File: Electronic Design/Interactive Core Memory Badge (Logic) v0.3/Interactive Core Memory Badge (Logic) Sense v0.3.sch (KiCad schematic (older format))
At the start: 22 parts, among them Q23 MMBT4401LT1G, Q24 MMBT4401LT1G, U3 LM393

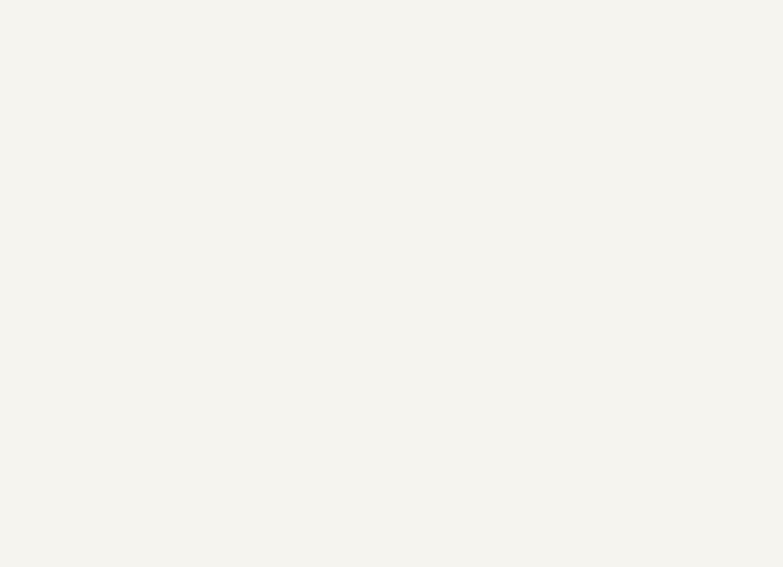
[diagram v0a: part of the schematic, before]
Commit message: Add I2C bus, clean-up power symbols, update MCU sheet.
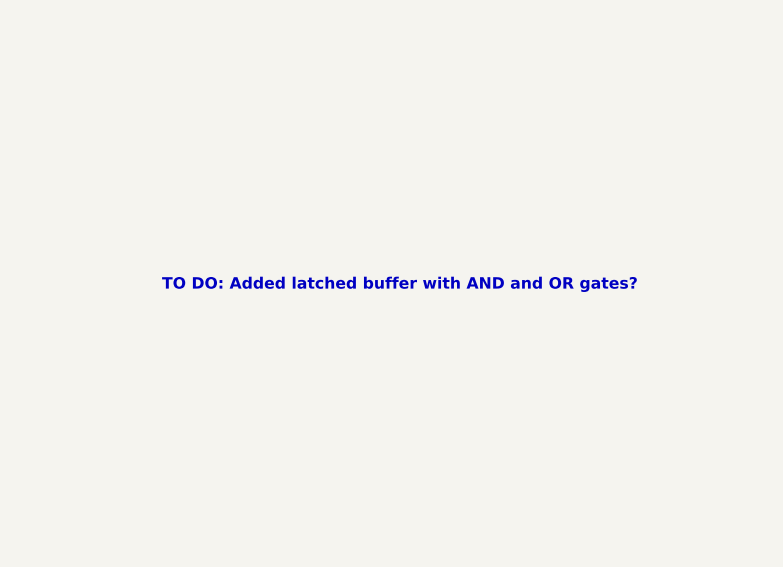
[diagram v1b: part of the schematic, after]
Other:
- note added: "TO DO: Added latched buffer with AND and OR gates?"
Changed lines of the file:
@@
 Connection ~ 3050 4850
 Connection ~ 3050 5450
+Text Notes 7200 3400 0    50   ~ 10
+TO DO: Added latched buffer with AND and OR gates?
 $EndSCHEMATC

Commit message: Add sense NORs and IO expansion and NOTs.
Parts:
- removed Q23, Q24: MMBT4401LT1G, Digikey:SOT-23-3, symbol Digikey-Transistors:MMBT4401LT1G
- removed R47: 10k, Resistor_SMD:R_0805_2012Metric, symbol Device:R
- added C7: 0.1uF, Capacitor_SMD:C_0805_2012Metric, symbol Device:CP1_Small
- added U4: 74HC02, symbol 74xx:74HC02
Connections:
- net labels added: 3V3_100mA, SENSE_RESET
- net labels removed: +3V3
- wire segments 63 -> 89
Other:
- note added: "SENSE SIGNAL RS LATCH"
- note removed: "SENSE SIGNAL BUFFER AND HOLD"
- note removed: "TO DO: Added latched buffer with AND and OR gates?"
- moved on the sheet: C4, C5, R36, R37, R38, R39, R40, R41, R42, R43, R44, R45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

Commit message: Schematic refinement
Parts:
- U4: footprint (none) -> Package_SO:SOIC-14_3.9x8.7mm_P1.27mm
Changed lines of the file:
@@
 $Descr A4 11693 8268
 encoding utf-8
-Sheet 5 6
+Sheet 3 5
 Title "Core 64 - Sense"
 Date "2020-03-15"
@@
 Comment4 ""
 $EndDescr
-Text Notes 550  700  0    118  ~ 0
+Text Notes 600  850  0    118  ~ 0
 SENSE SIGNAL PROCESSING
 $Comp
@@
 F 0 "U4" H 5100 2929 50  0000 C CNN
 F 1 "74HC02" H 5100 2836 50  0000 C CNN
-F 2 "" H 5100 2600 50  0001 C CNN
+F 2 "Package_SO:SOIC-14_3.9x8.7mm_P1.27mm" H 5100 2600 50  0001 C CNN
 F 3 "http://www.ti.com/lit/gpn/sn74hc02" H 5100 2600 50  0001 C CNN
 	1    5100 2600
@@
 F 0 "U4" H 5800 2929 50  0000 C CNN
 F 1 "74HC02" H 5800 2836 50  0000 C CNN
-F 2 "" H 5800 2600 50  0001 C CNN
+F 2 "Package_SO:SOIC-14_3.9x8.7mm_P1.27mm" H 5800 2600 50  0001 C CNN
 F 3 "http://www.ti.com/lit/gpn/sn74hc02" H 5800 2600 50  0001 C CNN
 	2    5800 2600
@@
 F 0 "U4" H 6500 2050 50  0000 C CNN
 F 1 "74HC02" H 6550 1950 50  0000 C CNN
-F 2 "" H 6600 1750 50  0001 C CNN
+F 2 "Package_SO:SOIC-14_3.9x8.7mm_P1.27mm" H 6600 1750 50  0001 C CNN
 F 3 "http://www.ti.com/lit/gpn/sn74hc02" H 6600 1750 50  0001 C CNN
 	3    6600 1750
@@
 F 0 "U4" H 6500 2800 50  0000 C CNN
 F 1 "74HC02" H 6550 2700 50  0000 C CNN
-F 2 "" H 6600 2500 50  0001 C CNN
+F 2 "Package_SO:SOIC-14_3.9x8.7mm_P1.27mm" H 6600 2500 50  0001 C CNN
 F 3 "http://www.ti.com/lit/gpn/sn74hc02" H 6600 2500 50  0001 C CNN
 	4    6600 2500
@@
 F 0 "U4" H 5380 3697 50  0000 L CNN
 F 1 "74HC02" H 5380 3604 50  0000 L CNN
-F 2 "" H 5150 3650 50  0001 C CNN
+F 2 "Package_SO:SOIC-14_3.9x8.7mm_P1.27mm" H 5150 3650 50  0001 C CNN
 F 3 "http://www.ti.com/lit/gpn/sn74hc02" H 5150 3650 50  0001 C CNN
 	5    5150 3650

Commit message: Overall PCB layout placements
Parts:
- removed TP18: SENSE1, TestPoint:TestPoint_Keystone_5000-5004_Miniature, symbol Connector:TestPoint
- removed TP19: SENSE2, TestPoint:TestPoint_Keystone_5000-5004_Miniature, symbol Connector:TestPoint
- removed TP20: SENSE_OUT_A, TestPoint:TestPoint_Keystone_5000-5004_Miniature, symbol Connector:TestPoint
- removed TP21: SENSE_OUT_B, TestPoint:TestPoint_Keystone_5000-5004_Miniature, symbol Connector:TestPoint
- removed TP22: SENSE_PULSE, TestPoint:TestPoint_Keystone_5000-5004_Miniature, symbol Connector:TestPoint
- added J6: Conn_01x08_Female, Connector_PinSocket_2.54mm:PinSocket_1x08_P2.54mm_Vertical, symbol Connector:Conn_01x08_Female
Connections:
- net GNDD: now also J6.1 (Pin_1)
- net SENSE1: now also J6.3 (Pin_3)
- net SENSE2: now also J6.4 (Pin_4)
- net SENSE_PULSE: now also J6.8 (Pin_8)
- net SENSE_RESET: now also J6.7 (Pin_7)
- net SENSE_OUT_B: now reaches R44.2, R46.2, U3.7
- net SENSE_OUT_B: now also J6.6 (Pin_6)
- net SENSE_OUT_A: now reaches R43.2, R45.2, U3.1
- net SENSE_OUT_A: now also J6.5 (Pin_5)
- net 3V3_100mA renamed 3V3_800mA
- net 3V3_800mA: now also J6.2 (Pin_2)
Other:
- note added: "SENSE DEBUG SOCKET"
- moved on the sheet: C4, C5, C7, U3C, U4E

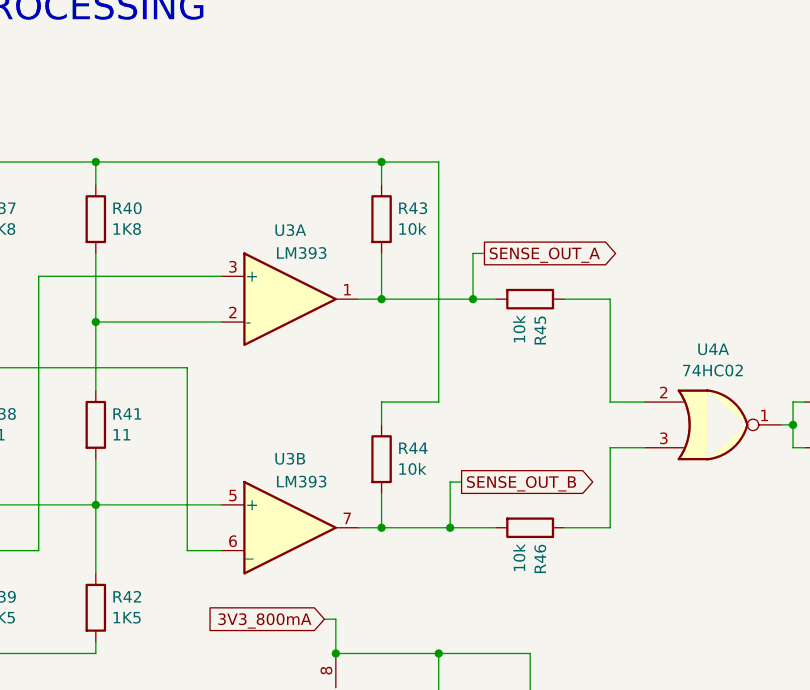
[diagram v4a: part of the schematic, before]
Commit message: Board layout, PDFs for review
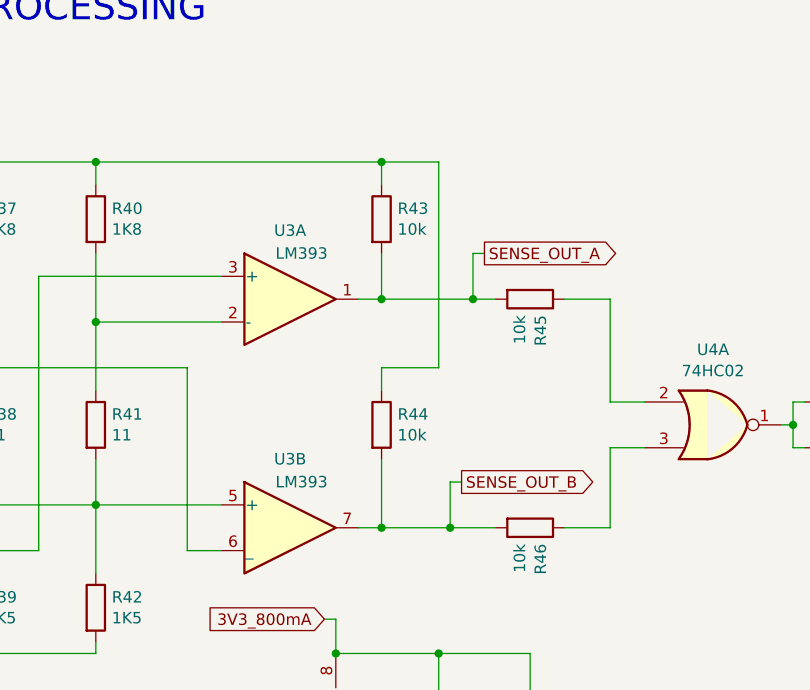
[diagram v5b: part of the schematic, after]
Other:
- moved on the sheet: R44
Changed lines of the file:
@@
 L Device:R R44
 U 1 1 5E624389
-P 3650 2750
-F 0 "R44" H 3720 2796 50  0000 L CNN
-F 1 "10k" H 3720 2705 50  0000 L CNN
-F 2 "Resistor_SMD:R_0805_2012Metric" V 3580 2750 50  0001 C CNN
-F 3 "~" H 3650 2750 50  0001 C CNN
-	1    3650 2750
-	1    0    0    -1
-$EndComp
-Wire Wire Line
-	3650 2900 3650 3050
+P 3650 2600
+F 0 "R44" H 3720 2646 50  0000 L CNN
+F 1 "10k" H 3720 2555 50  0000 L CNN
+F 2 "Resistor_SMD:R_0805_2012Metric" V 3580 2600 50  0001 C CNN
+F 3 "~" H 3650 2600 50  0001 C CNN
+	1    3650 2600
+	1    0    0    -1
+$EndComp
+Wire Wire Line
+	3650 2750 3650 3050
 Connection ~ 3650 3050
 Wire Wire Line
@@
 	3650 1550 3650 1450
 Wire Wire Line
-	3650 2500 3650 2600
+	3650 2350 3650 2450
 Wire Wire Line
 	3450 3600 3450 3450
@@
 	2400 1450 3650 1450
 Wire Wire Line
-	3650 2500 3900 2500
-Wire Wire Line
-	3900 2500 3900 1450
+	3650 2350 3900 2350
+Wire Wire Line
+	3900 2350 3900 1450
 Wire Wire Line
 	3900 1450 3650 1450

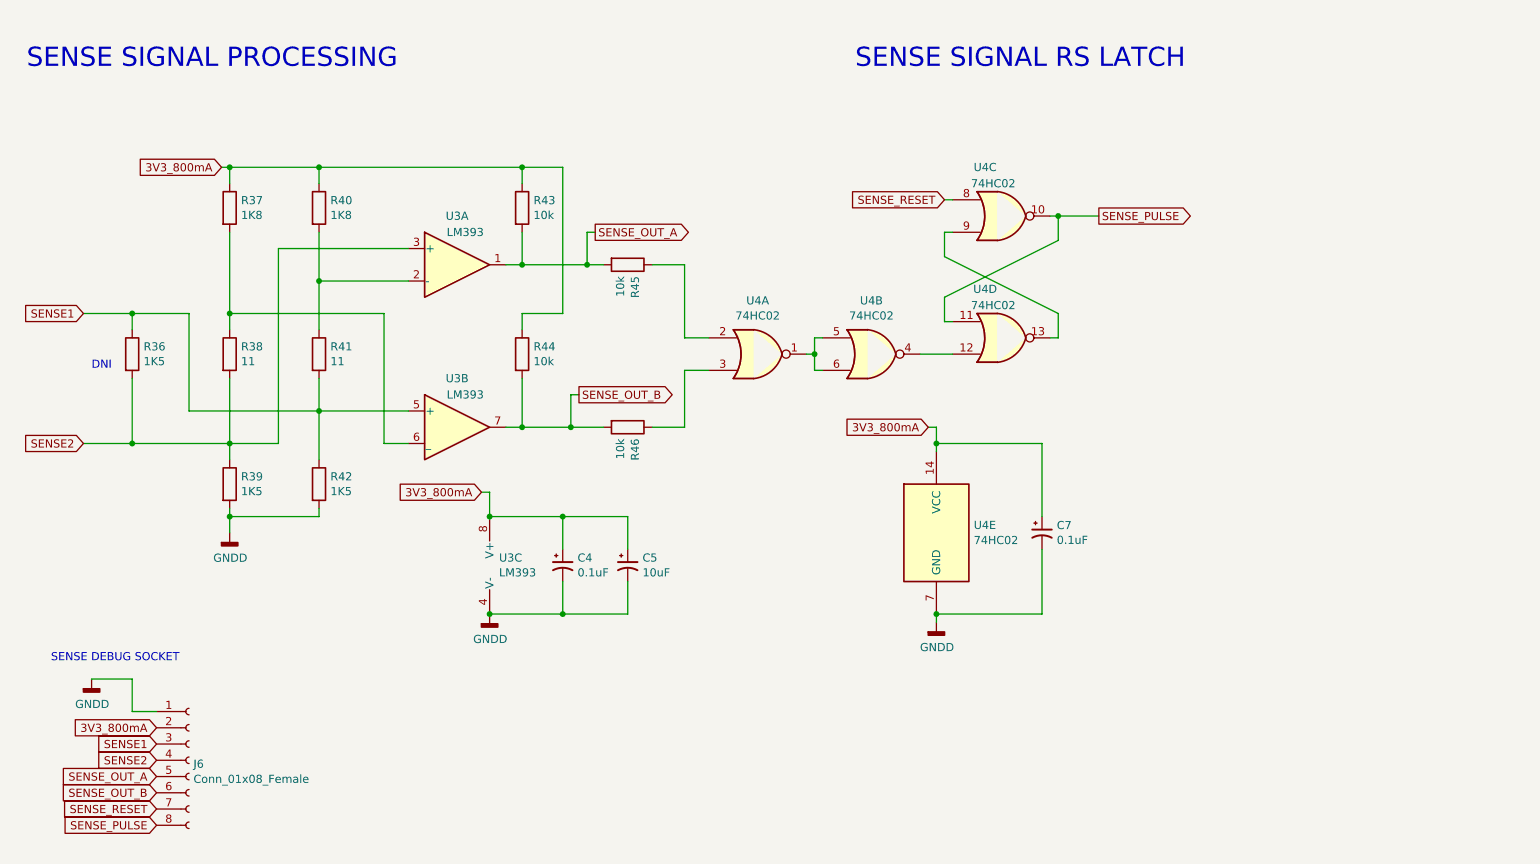
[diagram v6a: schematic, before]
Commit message: Logic board layout power routing
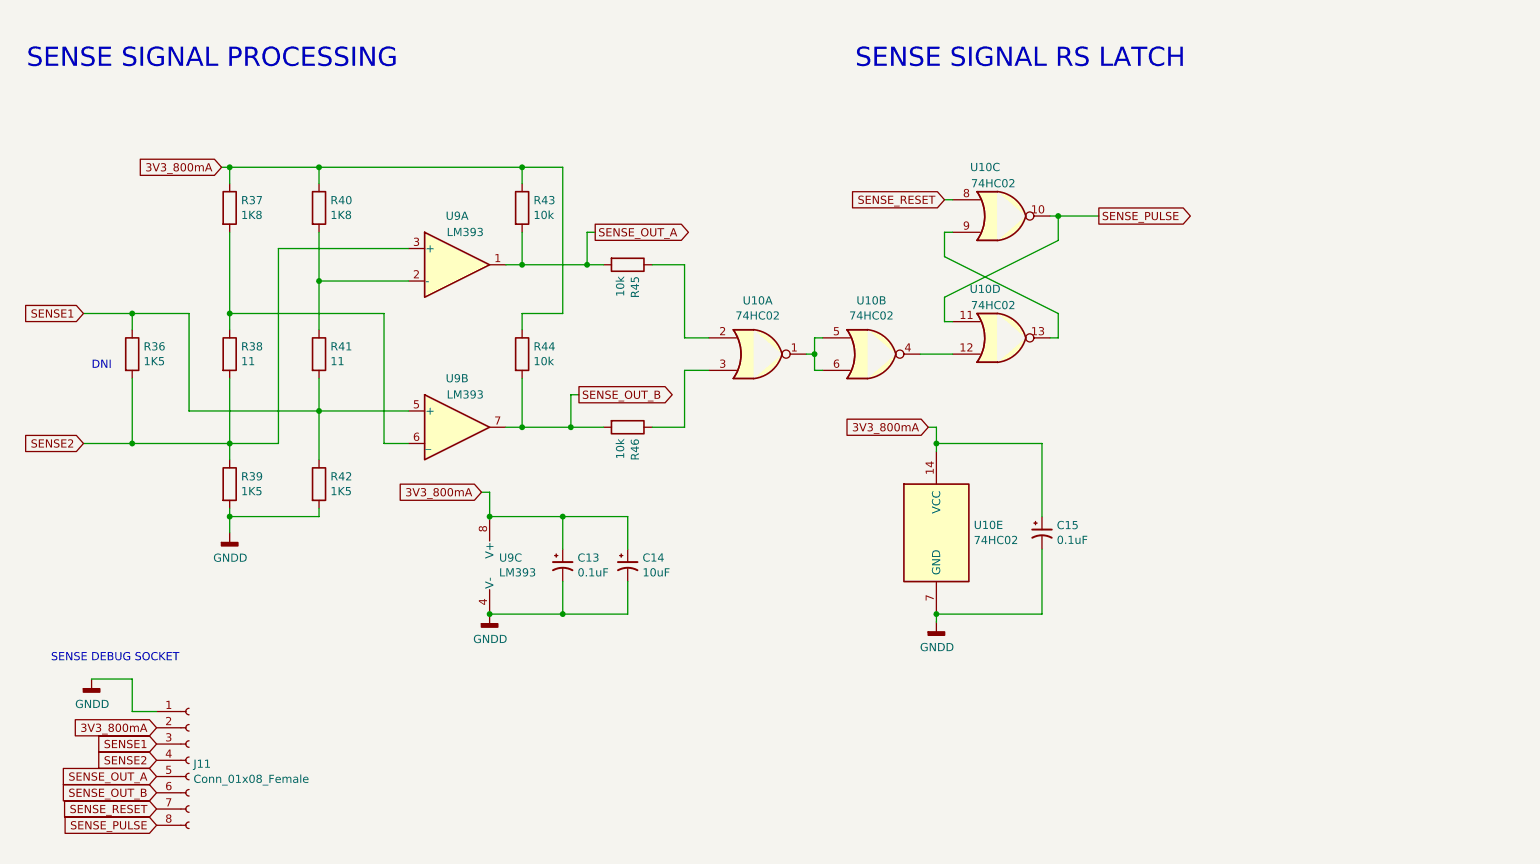
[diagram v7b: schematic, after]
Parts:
- renumbered C4 to C13, C5 to C14, C7 to C15, J6 to J11, U4 to U10, U3 to U9
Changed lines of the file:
@@
 AR Path="/5D2551FF/5D3DC9EC" Ref="U3"  Part="1"
 AR Path="/5E755787/5D3DC9EC" Ref="U?"  Part="1"
-AR Path="/5E75D6AB/5D3DC9EC" Ref="U3"  Part="1"
-F 0 "U3" H 3250 2350 50  0000 C CNN
+AR Path="/5E75D6AB/5D3DC9EC" Ref="U9"  Part="1"
+F 0 "U9" H 3250 2350 50  0000 C CNN
 F 1 "LM393" H 3300 2250 50  0000 C CNN
 F 2 "Digikey:SOIC-8_W3.9mm" H 3250 2050 50  0001 C CNN
@@
 	1850 2350 1850 2450
 $Comp
-L Comparator:LM393 U3
+L Comparator:LM393 U9
 U 2 1 5D3C9C38
 P 3250 3050
-F 0 "U3" H 3250 3350 50  0000 C CNN
+F 0 "U9" H 3250 3350 50  0000 C CNN
 F 1 "LM393" H 3300 3250 50  0000 C CNN
 F 2 "Digikey:SOIC-8_W3.9mm" H 3250 3050 50  0001 C CNN
@@
 $EndComp
 $Comp
-L Comparator:LM393 U3
+L Comparator:LM393 U9
 U 3 1 5D3CAF67
 P 3550 3900
-F 0 "U3" H 3508 3946 50  0000 L CNN
+F 0 "U9" H 3508 3946 50  0000 L CNN
 F 1 "LM393" H 3508 3855 50  0000 L CNN
 F 2 "Digikey:SOIC-8_W3.9mm" H 3550 3900 50  0001 C CNN
@@
 DNI
 $Comp
-L Device:CP1_Small C4
+L Device:CP1_Small C13
 U 1 1 5E6F58E8
 P 3900 3900
-F 0 "C4" H 3991 3946 50  0000 L CNN
+F 0 "C13" H 3991 3946 50  0000 L CNN
 F 1 "0.1uF" H 3991 3855 50  0000 L CNN
 F 2 "Capacitor_SMD:C_0805_2012Metric" H 3900 3900 50  0001 C CNN
@@
 $EndComp
 $Comp
-L Device:CP1_Small C5
+L Device:CP1_Small C14
 U 1 1 5E6F8864
 P 4300 3900
-F 0 "C5" H 4391 3946 50  0000 L CNN
+F 0 "C14" H 4391 3946 50  0000 L CNN
 F 1 "10uF" H 4391 3855 50  0000 L CNN
 F 2 "Capacitor_SMD:C_0805_2012Metric" H 4300 3900 50  0001 C CNN
@@
 SENSE_PULSE
 $Comp
-L 74xx:74HC02 U4
+L 74xx:74HC02 U10
 U 1 1 5E7CE53C
 P 5100 2600
-F 0 "U4" H 5100 2929 50  0000 C CNN
+F 0 "U10" H 5100 2929 50  0000 C CNN
 F 1 "74HC02" H 5100 2836 50  0000 C CNN
 F 2 "Package_SO:SOIC-14_3.9x8.7mm_P1.27mm" H 5100 2600 50  0001 C CNN
@@
 $EndComp
 $Comp
-L 74xx:74HC02 U4
+L 74xx:74HC02 U10
 U 2 1 5E7D6166
 P 5800 2600
-F 0 "U4" H 5800 2929 50  0000 C CNN
+F 0 "U10" H 5800 2929 50  0000 C CNN
 F 1 "74HC02" H 5800 2836 50  0000 C CNN
 F 2 "Package_SO:SOIC-14_3.9x8.7mm_P1.27mm" H 5800 2600 50  0001 C CNN
@@
 $EndComp
 $Comp
-L 74xx:74HC02 U4
+L 74xx:74HC02 U10
 U 3 1 5E7DA182
 P 6600 1750
-F 0 "U4" H 6500 2050 50  0000 C CNN
+F 0 "U10" H 6500 2050 50  0000 C CNN
 F 1 "74HC02" H 6550 1950 50  0000 C CNN
 F 2 "Package_SO:SOIC-14_3.9x8.7mm_P1.27mm" H 6600 1750 50  0001 C CNN
@@
 $EndComp
 $Comp
-L 74xx:74HC02 U4
+L 74xx:74HC02 U10
 U 4 1 5E7DD8C9
 P 6600 2500
-F 0 "U4" H 6500 2800 50  0000 C CNN
+F 0 "U10" H 6500 2800 50  0000 C CNN
 F 1 "74HC02" H 6550 2700 50  0000 C CNN
 F 2 "Package_SO:SOIC-14_3.9x8.7mm_P1.27mm" H 6600 2500 50  0001 C CNN
@@
 $EndComp
 $Comp
-L 74xx:74HC02 U4
+L 74xx:74HC02 U10
 U 5 1 5E7E6F63
 P 6200 3700
-F 0 "U4" H 6430 3747 50  0000 L CNN
+F 0 "U10" H 6430 3747 50  0000 L CNN
 F 1 "74HC02" H 6430 3654 50  0000 L CNN
 F 2 "Package_SO:SOIC-14_3.9x8.7mm_P1.27mm" H 6200 3700 50  0001 C CNN
@@
 	6100 2600 6300 2600
 $Comp
-L Device:CP1_Small C7
+L Device:CP1_Small C15
 U 1 1 5E84C4A5
 P 6850 3700
-F 0 "C7" H 6941 3746 50  0000 L CNN
+F 0 "C15" H 6941 3746 50  0000 L CNN
 F 1 "0.1uF" H 6941 3655 50  0000 L CNN
 F 2 "Capacitor_SMD:C_0805_2012Metric" H 6850 3700 50  0001 C CNN
@@
 	2400 1450 1850 1450
 $Comp
-L Connector:Conn_01x08_Female J6
+L Connector:Conn_01x08_Female J11
 U 1 1 5E868B9C
 P 1600 5100
-F 0 "J6" H 1627 5077 50  0000 L CNN
+F 0 "J11" H 1627 5077 50  0000 L CNN
 F 1 "Conn_01x08_Female" H 1627 4984 50  0000 L CNN
 F 2 "Connector_PinSocket_2.54mm:PinSocket_1x08_P2.54mm_Vertical" H 1600 5100 50  0001 C CNN

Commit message: V0.3 Logic Board released for prototype!
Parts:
- renumbered C14 to C10, C15 to C11, C13 to C9, J11 to J8, U9 to U7, U10 to U8
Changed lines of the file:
@@
 Sheet 3 5
 Title "Core 64 - Sense"
-Date "2020-04-24"
+Date "2020-05-18"
 Rev "0.3"
 Comp "Andy Geppert - Machine Ideas, LLC"
@@
 AR Path="/5D2551FF/5D3DC9EC" Ref="U3"  Part="1"
 AR Path="/5E755787/5D3DC9EC" Ref="U?"  Part="1"
-AR Path="/5E75D6AB/5D3DC9EC" Ref="U9"  Part="1"
-F 0 "U9" H 3250 2350 50  0000 C CNN
+AR Path="/5E75D6AB/5D3DC9EC" Ref="U7"  Part="1"
+F 0 "U7" H 3250 2350 50  0000 C CNN
 F 1 "LM393" H 3300 2250 50  0000 C CNN
 F 2 "Digikey:SOIC-8_W3.9mm" H 3250 2050 50  0001 C CNN
@@
 	1850 2350 1850 2450
 $Comp
-L Comparator:LM393 U9
+L Comparator:LM393 U7
 U 2 1 5D3C9C38
 P 3250 3050
-F 0 "U9" H 3250 3350 50  0000 C CNN
+F 0 "U7" H 3250 3350 50  0000 C CNN
 F 1 "LM393" H 3300 3250 50  0000 C CNN
 F 2 "Digikey:SOIC-8_W3.9mm" H 3250 3050 50  0001 C CNN
@@
 $EndComp
 $Comp
-L Comparator:LM393 U9
+L Comparator:LM393 U7
 U 3 1 5D3CAF67
 P 3550 3900
-F 0 "U9" H 3508 3946 50  0000 L CNN
+F 0 "U7" H 3508 3946 50  0000 L CNN
 F 1 "LM393" H 3508 3855 50  0000 L CNN
 F 2 "Digikey:SOIC-8_W3.9mm" H 3550 3900 50  0001 C CNN
@@
 DNI
 $Comp
-L Device:CP1_Small C13
+L Device:CP1_Small C9
 U 1 1 5E6F58E8
 P 3900 3900
-F 0 "C13" H 3991 3946 50  0000 L CNN
+F 0 "C9" H 3991 3946 50  0000 L CNN
 F 1 "0.1uF" H 3991 3855 50  0000 L CNN
 F 2 "Capacitor_SMD:C_0805_2012Metric" H 3900 3900 50  0001 C CNN
@@
 $EndComp
 $Comp
-L Device:CP1_Small C14
+L Device:CP1_Small C10
 U 1 1 5E6F8864
 P 4300 3900
-F 0 "C14" H 4391 3946 50  0000 L CNN
+F 0 "C10" H 4391 3946 50  0000 L CNN
 F 1 "10uF" H 4391 3855 50  0000 L CNN
 F 2 "Capacitor_SMD:C_0805_2012Metric" H 4300 3900 50  0001 C CNN
@@
 SENSE_PULSE
 $Comp
-L 74xx:74HC02 U10
+L 74xx:74HC02 U8
 U 1 1 5E7CE53C
 P 5100 2600
-F 0 "U10" H 5100 2929 50  0000 C CNN
+F 0 "U8" H 5100 2929 50  0000 C CNN
 F 1 "74HC02" H 5100 2836 50  0000 C CNN
 F 2 "Package_SO:SOIC-14_3.9x8.7mm_P1.27mm" H 5100 2600 50  0001 C CNN
@@
 $EndComp
 $Comp
-L 74xx:74HC02 U10
+L 74xx:74HC02 U8
 U 2 1 5E7D6166
 P 5800 2600
-F 0 "U10" H 5800 2929 50  0000 C CNN
+F 0 "U8" H 5800 2929 50  0000 C CNN
 F 1 "74HC02" H 5800 2836 50  0000 C CNN
 F 2 "Package_SO:SOIC-14_3.9x8.7mm_P1.27mm" H 5800 2600 50  0001 C CNN
@@
 $EndComp
 $Comp
-L 74xx:74HC02 U10
+L 74xx:74HC02 U8
 U 3 1 5E7DA182
 P 6600 1750
-F 0 "U10" H 6500 2050 50  0000 C CNN
+F 0 "U8" H 6500 2050 50  0000 C CNN
 F 1 "74HC02" H 6550 1950 50  0000 C CNN
 F 2 "Package_SO:SOIC-14_3.9x8.7mm_P1.27mm" H 6600 1750 50  0001 C CNN
@@
 $EndComp
 $Comp
-L 74xx:74HC02 U10
+L 74xx:74HC02 U8
 U 4 1 5E7DD8C9
 P 6600 2500
-F 0 "U10" H 6500 2800 50  0000 C CNN
+F 0 "U8" H 6500 2800 50  0000 C CNN
 F 1 "74HC02" H 6550 2700 50  0000 C CNN
 F 2 "Package_SO:SOIC-14_3.9x8.7mm_P1.27mm" H 6600 2500 50  0001 C CNN
@@
 $EndComp
 $Comp
-L 74xx:74HC02 U10
+L 74xx:74HC02 U8
 U 5 1 5E7E6F63
 P 6200 3700
-F 0 "U10" H 6430 3747 50  0000 L CNN
+F 0 "U8" H 6430 3747 50  0000 L CNN
 F 1 "74HC02" H 6430 3654 50  0000 L CNN
 F 2 "Package_SO:SOIC-14_3.9x8.7mm_P1.27mm" H 6200 3700 50  0001 C CNN
@@
 	6100 2600 6300 2600
 $Comp
-L Device:CP1_Small C15
+L Device:CP1_Small C11
 U 1 1 5E84C4A5
 P 6850 3700
-F 0 "C15" H 6941 3746 50  0000 L CNN
+F 0 "C11" H 6941 3746 50  0000 L CNN
 F 1 "0.1uF" H 6941 3655 50  0000 L CNN
 F 2 "Capacitor_SMD:C_0805_2012Metric" H 6850 3700 50  0001 C CNN
@@
 	2400 1450 1850 1450
 $Comp
-L Connector:Conn_01x08_Female J11
+L Connector:Conn_01x08_Female J8
 U 1 1 5E868B9C
 P 1600 5100
-F 0 "J11" H 1627 5077 50  0000 L CNN
+F 0 "J8" H 1627 5077 50  0000 L CNN
 F 1 "Conn_01x08_Female" H 1627 4984 50  0000 L CNN
 F 2 "Connector_PinSocket_2.54mm:PinSocket_1x08_P2.54mm_Vertical" H 1600 5100 50  0001 C CNN
